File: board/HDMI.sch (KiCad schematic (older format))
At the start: 91 parts, among them J2 HDMI, J3 HDMI, J4 HDMI, J5 HDMI, P10 CONN_1, P19 CONN_1, P2 CONN_1, P20 CONN_1, P21 CONN_1, P22 CONN_1, P23 CONN_1, P24 CONN_1, P25 CONN_1, P26 CONN_1, P4 CONN_1, P5 CONN_1, P6 CONN_1, P7 CONN_1, P8 CONN_1, P9 CONN_1, U13 IP4776CZ38, U14 IP4776CZ38, U15 IP4776CZ38, U16 ΜA78L00, U21 IP4776CZ38, U22 ΜA78L00, U30 ΜA78L00

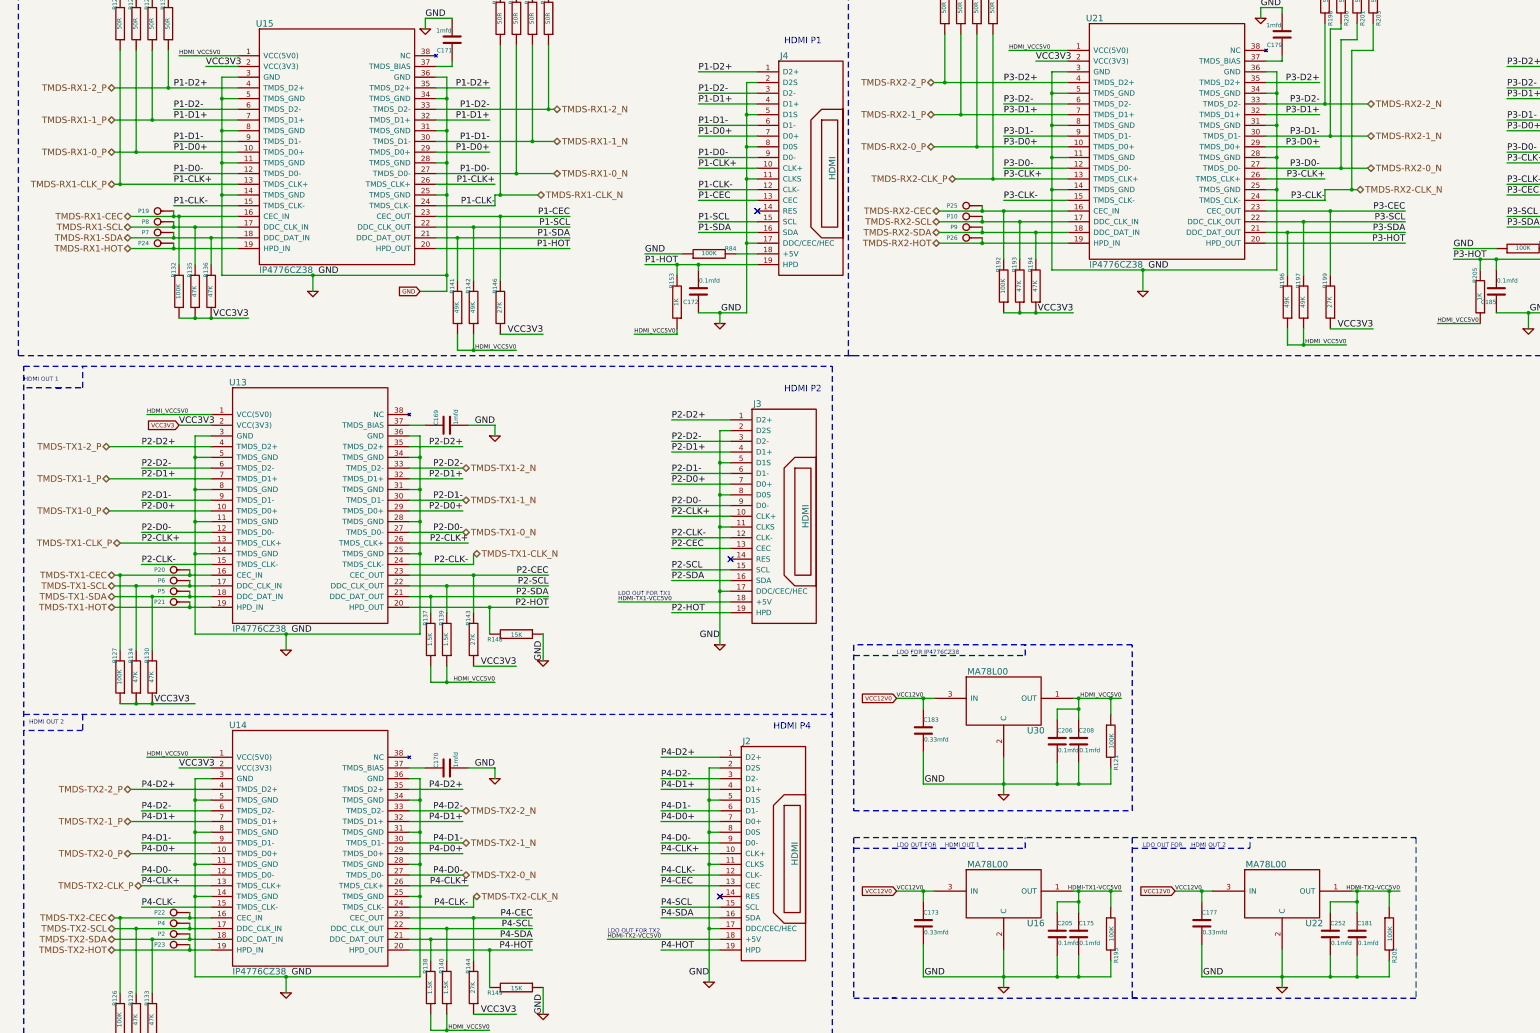
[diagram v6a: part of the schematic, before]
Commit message: Fix the signal name changing.
Fixes #23.
https://github.com/timvideos/HDMI2USB-numato-opsis-hardware/issues/23
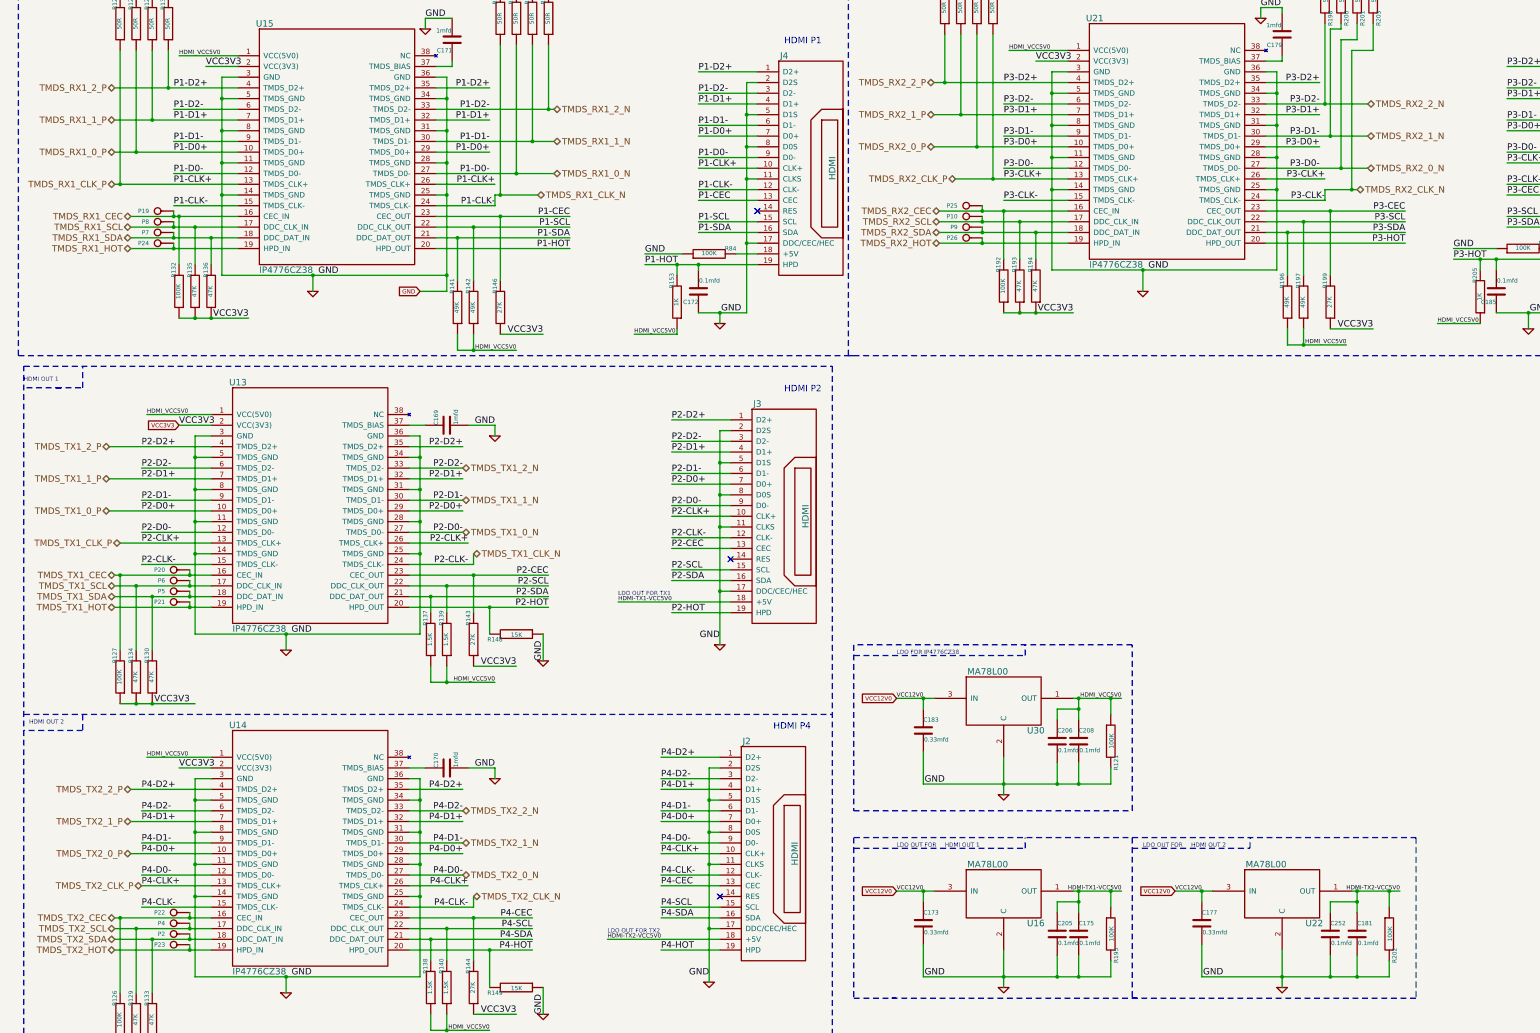
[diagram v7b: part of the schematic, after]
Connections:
- net TMDS-RX1-0_N renamed TMDS_RX1_0_N
- net TMDS-RX1-0_P renamed TMDS_RX1_0_P
- net TMDS-RX1-1_N renamed TMDS_RX1_1_N
- net TMDS-RX1-1_P renamed TMDS_RX1_1_P
- net TMDS-RX1-2_N renamed TMDS_RX1_2_N
- net TMDS-RX1-2_P renamed TMDS_RX1_2_P
- net TMDS-RX1-CEC renamed TMDS_RX1_CEC
- net TMDS-RX1-CLK_N renamed TMDS_RX1_CLK_N
- net TMDS-RX1-CLK_P renamed TMDS_RX1_CLK_P
- net TMDS-RX1-HOT renamed TMDS_RX1_HOT
- net TMDS-RX1-SCL renamed TMDS_RX1_SCL
- net TMDS-RX1-SDA renamed TMDS_RX1_SDA
- net TMDS-RX2-0_N renamed TMDS_RX2_0_N
- net TMDS-RX2-0_P renamed TMDS_RX2_0_P
- net TMDS-RX2-1_N renamed TMDS_RX2_1_N
- net TMDS-RX2-1_P renamed TMDS_RX2_1_P
- net TMDS-RX2-2_N renamed TMDS_RX2_2_N
- net TMDS-RX2-2_P renamed TMDS_RX2_2_P
- net TMDS-RX2-CEC renamed TMDS_RX2_CEC
- net TMDS-RX2-CLK_N renamed TMDS_RX2_CLK_N
- net TMDS-RX2-CLK_P renamed TMDS_RX2_CLK_P
- net TMDS-RX2-HOT renamed TMDS_RX2_HOT
- net TMDS-RX2-SCL renamed TMDS_RX2_SCL
- net TMDS-RX2-SDA renamed TMDS_RX2_SDA
- net TMDS-TX1-0_N renamed TMDS_TX1_0_N
- net TMDS-TX1-0_P renamed TMDS_TX1_0_P
- net TMDS-TX1-1_N renamed TMDS_TX1_1_N
- net TMDS-TX1-1_P renamed TMDS_TX1_1_P
- net TMDS-TX1-2_N renamed TMDS_TX1_2_N
- net TMDS-TX1-2_P renamed TMDS_TX1_2_P
- net TMDS-TX1-CEC renamed TMDS_TX1_CEC
- net TMDS-TX1-CLK_N renamed TMDS_TX1_CLK_N
- net TMDS-TX1-CLK_P renamed TMDS_TX1_CLK_P
- net TMDS-TX1-HOT renamed TMDS_TX1_HOT
- net TMDS-TX1-SCL renamed TMDS_TX1_SCL
- net TMDS-TX1-SDA renamed TMDS_TX1_SDA
- net TMDS-TX2-0_N renamed TMDS_TX2_0_N
- net TMDS-TX2-0_P renamed TMDS_TX2_0_P
- net TMDS-TX2-1_N renamed TMDS_TX2_1_N
- net TMDS-TX2-1_P renamed TMDS_TX2_1_P
- net TMDS-TX2-2_N renamed TMDS_TX2_2_N
- net TMDS-TX2-2_P renamed TMDS_TX2_2_P
- net TMDS-TX2-CEC renamed TMDS_TX2_CEC
- net TMDS-TX2-CLK_N renamed TMDS_TX2_CLK_N
- net TMDS-TX2-CLK_P renamed TMDS_TX2_CLK_P
- net TMDS-TX2-HOT renamed TMDS_TX2_HOT
- net TMDS-TX2-SCL renamed TMDS_TX2_SCL
- net TMDS-TX2-SDA renamed TMDS_TX2_SDA
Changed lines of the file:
@@
 P1-CLK+
 Text HLabel 1400 2000 0    60   BiDi ~ 0
-TMDS-RX1-2_P
+TMDS_RX1_2_P
 Text HLabel 1400 2300 0    60   BiDi ~ 0
-TMDS-RX1-1_P
+TMDS_RX1_1_P
 Text HLabel 1400 2600 0    60   BiDi ~ 0
-TMDS-RX1-0_P
+TMDS_RX1_0_P
 Text HLabel 5500 2200 2    60   BiDi ~ 0
-TMDS-RX1-2_N
+TMDS_RX1_2_N
 Text HLabel 5500 2500 2    60   BiDi ~ 0
-TMDS-RX1-1_N
+TMDS_RX1_1_N
 Text HLabel 5500 2800 2    60   BiDi ~ 0
-TMDS-RX1-0_N
+TMDS_RX1_0_N
 Text HLabel 1400 2900 0    60   BiDi ~ 0
-TMDS-RX1-CLK_P
+TMDS_RX1_CLK_P
 Text HLabel 5350 3000 2    60   BiDi ~ 0
-TMDS-RX1-CLK_N
+TMDS_RX1_CLK_N
 NoConn ~ 7400 3150
 Text HLabel 1550 3300 0    60   BiDi ~ 0
-TMDS-RX1-SCL
+TMDS_RX1_SCL
 Text HLabel 1550 3400 0    60   BiDi ~ 0
-TMDS-RX1-SDA
+TMDS_RX1_SDA
 $Comp
 L HDMI J3
@@
 P2-CLK+
 Text HLabel 1350 5350 0    60   BiDi ~ 0
-TMDS-TX1-2_P
+TMDS_TX1_2_P
 Text HLabel 1350 5650 0    60   BiDi ~ 0
-TMDS-TX1-1_P
+TMDS_TX1_1_P
 Text HLabel 1350 5950 0    60   BiDi ~ 0
-TMDS-TX1-0_P
+TMDS_TX1_0_P
 Text HLabel 4650 5550 2    60   BiDi ~ 0
-TMDS-TX1-2_N
+TMDS_TX1_2_N
 Text HLabel 4650 5850 2    60   BiDi ~ 0
-TMDS-TX1-1_N
+TMDS_TX1_1_N
 Text HLabel 4650 6150 2    60   BiDi ~ 0
-TMDS-TX1-0_N
+TMDS_TX1_0_N
 Text HLabel 1450 6250 0    60   BiDi ~ 0
-TMDS-TX1-CLK_P
+TMDS_TX1_CLK_P
 Text HLabel 4750 6350 2    60   BiDi ~ 0
-TMDS-TX1-CLK_N
+TMDS_TX1_CLK_N
 NoConn ~ 7150 6400
 $Comp
@@
 P4-CLK+
 Text HLabel 1550 8550 0    60   BiDi ~ 0
-TMDS-TX2-2_P
+TMDS_TX2_2_P
 Text HLabel 1550 8850 0    60   BiDi ~ 0
-TMDS-TX2-1_P
+TMDS_TX2_1_P
 Text HLabel 1550 9150 0    60   BiDi ~ 0
-TMDS-TX2-0_P
+TMDS_TX2_0_P
 Text HLabel 4650 8750 2    60   BiDi ~ 0
-TMDS-TX2-2_N
+TMDS_TX2_2_N
 Text HLabel 4650 9050 2    60   BiDi ~ 0
-TMDS-TX2-1_N
+TMDS_TX2_1_N
 Text HLabel 4650 9350 2    60   BiDi ~ 0
-TMDS-TX2-0_N
+TMDS_TX2_0_N
 Text HLabel 1650 9450 0    60   BiDi ~ 0
-TMDS-TX2-CLK_P
+TMDS_TX2_CLK_P
 Text HLabel 4750 9550 2    60   BiDi ~ 0
-TMDS-TX2-CLK_N
+TMDS_TX2_CLK_N
 NoConn ~ 7050 9550
 $Comp
@@
 VSS
 Text HLabel 9050 1950 0    60   BiDi ~ 0
-TMDS-RX2-2_P
+TMDS_RX2_2_P
 Text HLabel 9050 2250 0    60   BiDi ~ 0
-TMDS-RX2-1_P
+TMDS_RX2_1_P
 Text HLabel 9050 2550 0    60   BiDi ~ 0
-TMDS-RX2-0_P
+TMDS_RX2_0_P
 Text HLabel 13100 2150 2    60   BiDi ~ 0
-TMDS-RX2-2_N
+TMDS_RX2_2_N
 Text HLabel 13100 2450 2    60   BiDi ~ 0
-TMDS-RX2-1_N
+TMDS_RX2_1_N
 Text HLabel 13100 2750 2    60   BiDi ~ 0
-TMDS-RX2-0_N
+TMDS_RX2_0_N
 Text HLabel 9250 2850 0    60   BiDi ~ 0
-TMDS-RX2-CLK_P
+TMDS_RX2_CLK_P
 Text HLabel 13000 2950 2    60   BiDi ~ 0
-TMDS-RX2-CLK_N
+TMDS_RX2_CLK_N
 NoConn ~ 14950 3100
 Text HLabel 1400 6550 0    60   BiDi ~ 0
-TMDS-TX1-CEC
+TMDS_TX1_CEC
 $Comp
 L R R126
@@
 P4-HOT
 Text HLabel 1400 9750 0    60   BiDi ~ 0
-TMDS-TX2-CEC
+TMDS_TX2_CEC
 Text HLabel 1550 3200 0    60   BiDi ~ 0
-TMDS-RX1-CEC
+TMDS_RX1_CEC
 Text HLabel 9100 3150 0    60   BiDi ~ 0
-TMDS-RX2-CEC
+TMDS_RX2_CEC
 Text HLabel 9100 3250 0    60   BiDi ~ 0
-TMDS-RX2-SCL
+TMDS_RX2_SCL
 Text HLabel 9100 3350 0    60   BiDi ~ 0
-TMDS-RX2-SDA
+TMDS_RX2_SDA
 Text HLabel 1400 6650 0    60   BiDi ~ 0
-TMDS-TX1-SCL
+TMDS_TX1_SCL
 Text HLabel 1400 6750 0    60   BiDi ~ 0
-TMDS-TX1-SDA
+TMDS_TX1_SDA
 Text HLabel 1400 6850 0    60   BiDi ~ 0
-TMDS-TX1-HOT
+TMDS_TX1_HOT
 Text HLabel 1400 9850 0    60   BiDi ~ 0
-TMDS-TX2-SCL
+TMDS_TX2_SCL
 Text HLabel 1400 9950 0    60   BiDi ~ 0
-TMDS-TX2-SDA
+TMDS_TX2_SDA
 Text HLabel 1400 10050 0    60   BiDi ~ 0
-TMDS-TX2-HOT
+TMDS_TX2_HOT
 Text HLabel 1550 3500 0    60   BiDi ~ 0
-TMDS-RX1-HOT
+TMDS_RX1_HOT
 Text HLabel 9100 3450 0    60   BiDi ~ 0
-TMDS-RX2-HOT
+TMDS_RX2_HOT
 $Comp
 L R R193
